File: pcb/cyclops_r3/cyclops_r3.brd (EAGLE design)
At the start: 69.8 x 53.3 mm, 78 parts, among them Q1 SUM11006, Q2 IRF540, U1 MCP4921, U2 317-N, U3 TLV37, U4 337-N, U5 ADR03, U6 OP1177, U7 TLV2374, U8 ZXTD45

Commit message: Minor fix to pcb.
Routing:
- net GND: track 102.9 -> 102.0 mm
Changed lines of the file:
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@@
 <layer number="27" name="tValues" color="7" fill="1" visible="yes" active="yes"/>
 <layer number="28" name="bValues" color="7" fill="1" visible="yes" active="yes"/>
-<layer number="29" name="tStop" color="7" fill="3" visible="no" active="yes"/>
-<layer number="30" name="bStop" color="7" fill="6" visible="no" active="yes"/>
+<layer number="29" name="tStop" color="7" fill="3" visible="yes" active="yes"/>
+<layer number="30" name="bStop" color="7" fill="6" visible="yes" active="yes"/>
 <layer number="31" name="tCream" color="7" fill="4" visible="no" active="yes"/>
 <layer number="32" name="bCream" color="7" fill="5" visible="no" active="yes"/>
@@
 <contactref element="C22" pad="2"/>
 <wire x1="15.875" y1="41.2496" x2="17.2974" y2="42.672" width="0.4064" layer="1"/>
-<wire x1="17.2974" y1="42.672" x2="18.796" y2="42.672" width="0.4064" layer="1"/>
-<wire x1="18.796" y1="42.672" x2="20.701" y2="42.672" width="0.4064" layer="1"/>
+<wire x1="17.2974" y1="42.672" x2="20.701" y2="42.672" width="0.4064" layer="1"/>
 <wire x1="20.701" y1="42.672" x2="20.955" y2="42.418" width="0.4064" layer="1"/>
 <wire x1="20.955" y1="42.418" x2="21.262" y2="42.418" width="0.4064" layer="1"/>
@@
 <wire x1="50.546" y1="37.719" x2="50.546" y2="39.37" width="0.8128" layer="1"/>
 <via x="40.64" y="43.688" extent="1-16" drill="0.9" shape="octagon"/>
-<wire x1="17.018" y1="43.942" x2="18.923" y2="42.799" width="0.4064" layer="1"/>
-<wire x1="18.923" y1="42.799" x2="18.796" y2="42.672" width="0.4064" layer="1" curve="-90"/>
+<wire x1="17.018" y1="43.942" x2="17.018" y2="43.053" width="0.4064" layer="1"/>
+<wire x1="17.018" y1="43.053" x2="17.399" y2="42.672" width="0.4064" layer="1"/>
 <wire x1="66.008" y1="11.459" x2="66.008" y2="11.144" width="0.4064" layer="1"/>
 <wire x1="58.547" y1="8.382" x2="58.166" y2="8.001" width="0.4064" layer="1"/>
@@
 <via x="38.989" y="30.226" extent="1-16" drill="0.9" shape="octagon"/>
 <wire x1="38.989" y1="28.575" x2="38.989" y2="30.226" width="0.8128" layer="1"/>
+<wire x1="17.399" y1="42.672" x2="17.2974" y2="42.672" width="0" layer="19" extent="1-1"/>
 </signal>
 <signal name="VIN">
@@
 </signal>
 </signals>
-<errors>
-</errors>
 </board>
 </drawing>

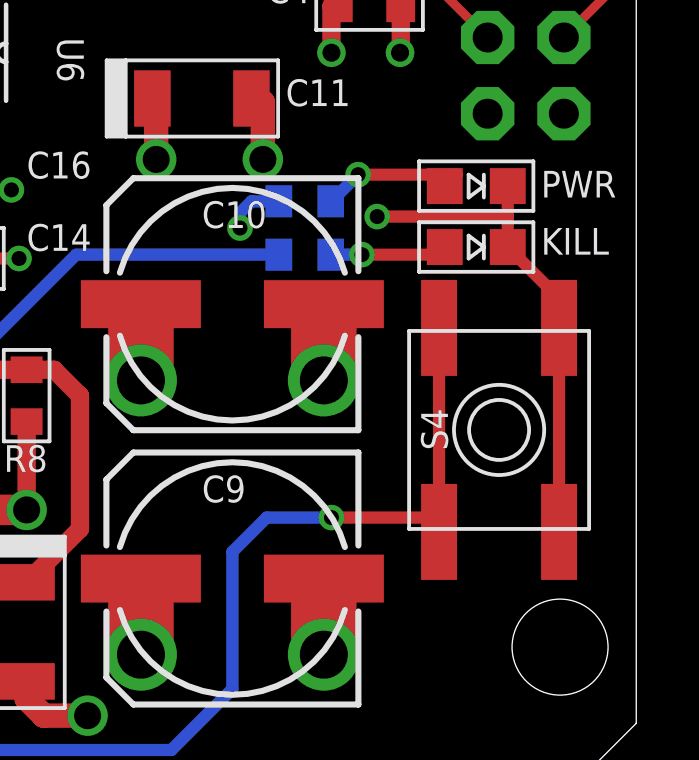
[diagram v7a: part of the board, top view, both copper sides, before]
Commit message: Finished up the BOM. Cleaned up the eagle library a bit.
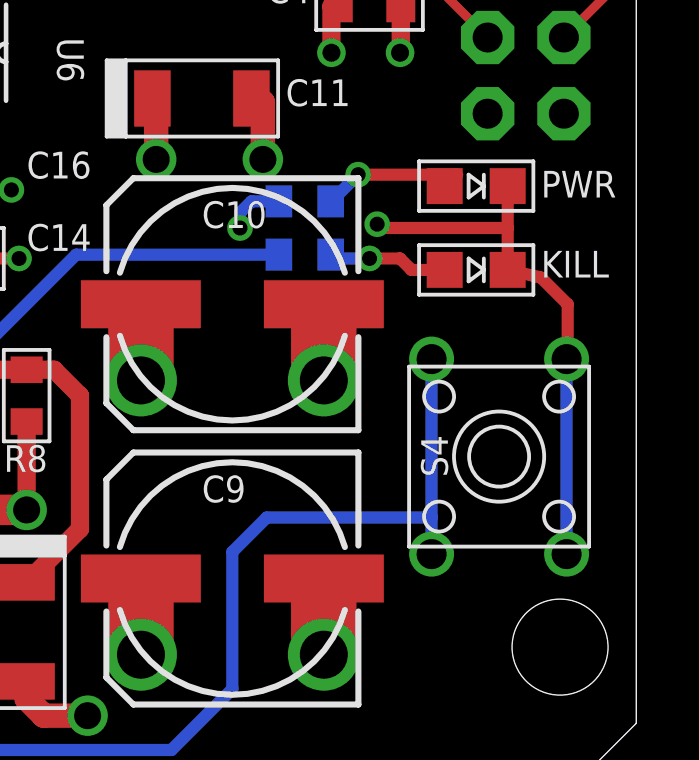
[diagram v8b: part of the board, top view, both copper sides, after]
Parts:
- C1, C21, R1: value ?? -> (none)
- C9: value 47uF -> 100uF
- KILL: value LED -> LEDRED
- PWR: value LED -> LEDGRN
- S4: device cyclops:EVQ-Q2 -> jonnew-eagle:B3F
- moved S4 0.89 mm to (64.0, 14.0)
- moved KILL 0.76 mm to (63.2, 20.2)
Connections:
- net COMP+: now also S4.1, S4.2; no longer S4.A, S4.A'
- net GND: now also S4.3, S4.4; no longer S4.B, S4.B'
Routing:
- net GND: track 102.0 -> 103.0 mm
- net COMP+: track 41.8 -> 41.1 mm, vias 1 -> 0
- added copper zone on layer 2, net N$14
